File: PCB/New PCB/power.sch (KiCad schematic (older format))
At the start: 3 parts

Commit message: Updating Schematic for New PCB
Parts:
- added SW1: SWITCH_INV, ~, symbol SWITCH_INV
- gave numbers to parts that had none: 3
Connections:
- net labels added: DIO10, DIO8, DIO9
- wire segments 10 -> 14
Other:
- moved on the sheet: P1
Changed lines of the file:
@@
-EESchema Schematic File Version 2  date 5/26/2013 8:12:24 PM
+EESchema Schematic File Version 2  date 5/27/2013 10:54:42 AM
 LIBS:power
 LIBS:device
@@
 LIBS:MyLib
 LIBS:Test-cache
-EELAYER 25  0
+EELAYER 27 0
 EELAYER END
-$Descr A4 11700 8267
+$Descr A4 11693 8268
 encoding utf-8
 Sheet 2 3
@@
 $EndDescr
 $Comp
-L CONN_2 P?
+L CONN_2 P1
 U 1 1 51A2B2CF
-P 1150 1600
-F 0 "P?" V 1100 1600 40  0000 C CNN
-F 1 "BATT_CONN" V 1200 1600 40  0000 C CNN
-	1    1150 1600
+P 1950 1800
+F 0 "P1" V 1900 1800 40  0000 C CNN
+F 1 "BATT_CONN" V 2000 1800 40  0000 C CNN
+F 2 "" H 1950 1800 60  0001 C CNN
+F 3 "" H 1950 1800 60  0001 C CNN
+	1    1950 1800
 	-1   0    0    1
 $EndComp
 $Comp
-L VCC #PWR?
+L VCC #PWR06
 U 1 1 51A2B2CE
 P 4800 1350
-F 0 "#PWR?" H 4800 1450 30  0001 C CNN
+F 0 "#PWR06" H 4800 1450 30  0001 C CNN
 F 1 "VCC" H 4800 1450 30  0000 C CNN
+F 2 "" H 4800 1350 60  0001 C CNN
+F 3 "" H 4800 1350 60  0001 C CNN
 	1    4800 1350
 	1    0    0    -1
 $EndComp
 $Comp
-L GND #PWR?
+L GND #PWR07
 U 1 1 51A2B2CD
 P 4100 2350
-F 0 "#PWR?" H 4100 2350 30  0001 C CNN
+F 0 "#PWR07" H 4100 2350 30  0001 C CNN
 F 1 "GND" H 4100 2280 30  0001 C CNN
+F 2 "" H 4100 2350 60  0001 C CNN
+F 3 "" H 4100 2350 60  0001 C CNN
 	1    4100 2350
 	1    0    0    -1
 $EndComp
 $Comp
-L C C?
+L C C1
 U 1 1 51A2B2CC
 P 4650 1850
-F 0 "C?" H 4650 1950 40  0000 L CNN
+F 0 "C1" H 4650 1950 40  0000 L CNN
 F 1 "C" H 4656 1765 40  0000 L CNN
 F 2 "~" H 4688 1700 30  0000 C CNN
@@
 $EndComp
 $Comp
-L REG1117 IC?
+L REG1117 3.3V1
 U 1 1 51A2B2CB
 P 4100 1650
-F 0 "IC?" H 4000 1900 60  0000 C CNN
+F 0 "3.3V1" H 4000 1900 60  0000 C CNN
 F 1 "REG1117" H 4150 1750 60  0000 C CNN
+F 2 "" H 4100 1650 60  0001 C CNN
+F 3 "" H 4100 1650 60  0001 C CNN
 	1    4100 1650
 	1    0    0    -1
@@
 	3850 1650 3650 1650
 Wire Wire Line
-	1600 1700 1600 2100
+	2400 1900 2400 2300
 Connection ~ 4100 2150
 Wire Wire Line
-	1600 1500 1500 1500
+	2400 1700 2300 1700
 Wire Wire Line
-	1500 1700 1600 1700
+	2300 1900 2400 1900
+$Comp
+L SWITCH_INV SW1
+U 1 1 51A3B93F
+P 2900 1700
+F 0 "SW1" H 2700 1850 50  0000 C CNN
+F 1 "SWITCH_INV" H 2750 1550 50  0000 C CNN
+F 2 "~" H 2900 1700 60  0000 C CNN
+F 3 "~" H 2900 1700 60  0000 C CNN
+	1    2900 1700
+	1    0    0    -1
+$EndComp
+Wire Wire Line
+	2400 2300 4100 2300
+Connection ~ 4100 2300
+Wire Wire Line
+	3400 1800 3400 2300
+Connection ~ 3400 2300
+Wire Wire Line
+	3400 1600 3650 1600
+Wire Wire Line
+	3650 1600 3650 1650
+Text HLabel 6900 3050 0    60   UnSpc ~ 0
+DIO8
+Text HLabel 6900 3150 0    60   UnSpc ~ 0
+DIO9
+Text HLabel 6900 3250 0    60   UnSpc ~ 0
+DIO10
 $EndSCHEMATC

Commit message: updated schematic
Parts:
- removed 3.3V1: REG1117, symbol REG1117
- removed C1: C, ~, symbol C
- removed SW1: SWITCH_INV, ~, symbol SWITCH_INV
- added C? (x2): 10uF, symbol CP1
- added C? (x11): 0.1uF, symbol C
- added C? (x2): 47uF, symbol C
- added C?: 10uF, symbol C
- added D?: LED, symbol LED
- added IC2?: REG1117, ~, symbol REG1117
- added R?: 320, symbol R
- added R?: 10, symbol R
- added SW?: SPST, symbol SPST
- added U? (x2): V78W-500, symbol V78W-500
- added U?: REC5-4805SRWZ/H4/A, symbol REC5-4805SRWZ/H4/A
- added U?: DSPIC33EP512MC806, ~, symbol DSPIC33EP512MC806
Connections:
- net labels added: +5V, Mag1_V, Mag2_V, Motor_Power, VSS
- wire segments 14 -> 37
- no-connect marks 0 -> 2
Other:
- note added: "24V DC DC converters for Magnets"
- note added: "3.3V Linear Regulator"
- note added: "45V-52V Input"
- note added: "5V DC-DC Isolation Converter, 1A max"
- moved on the sheet: P1

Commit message: more updates
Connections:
- net labels added: MotorPower
- net labels removed: DIO10, DIO8, DIO9, Motor_Power
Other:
- moved on the sheet: C?, R?, U?B

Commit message: updated schematic
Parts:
- removed C? (x4): 0.1uF, symbol C
- removed C? (x2): 47uF, symbol C
- removed U? (x2): V78W-500, symbol V78W-500
- removed U?: REC5-4805SRWZ/H4/A, symbol REC5-4805SRWZ/H4/A
- added C1, C2: 200uF, symbol C
- added C10, C7, C8, C9: 0.1uF, symbol C
- added C11, C12: 500uF, symbol C
- added C3, C6: C, symbol C
- added D6, D7: DIODESCH, symbol DIODESCH
- added L1, L2: INDUCTOR, symbol INDUCTOR
- added R20, R21, R22, R23, R3, R4: R, symbol R
- added U2, U3: 1074HV, symbol 1074HV
- gave numbers to parts that had none: 16
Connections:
- net labels added: +24V, +48V
- net labels removed: Mag1_V, Mag2_V, MotorPower, VSS
- wire segments 37 -> 42
- no-connect marks 2 -> 0
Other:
- note added: "24V DC DC buck converter"
- note added: "5V DC DC buck converter"
- note added: "Could use the fixed 5V Version (LT1076-5)"
- note added: "RIPPLE CURRENT RATING ≥ IOUT/2"
- note added: "dsPIC power pins"
- note removed: "24V DC DC converters for Magnets"
- note removed: "5V DC-DC Isolation Converter, 1A max"
- moved on the sheet: C13, C14, C34, C35, D8, IC21, P1, R24, SW1

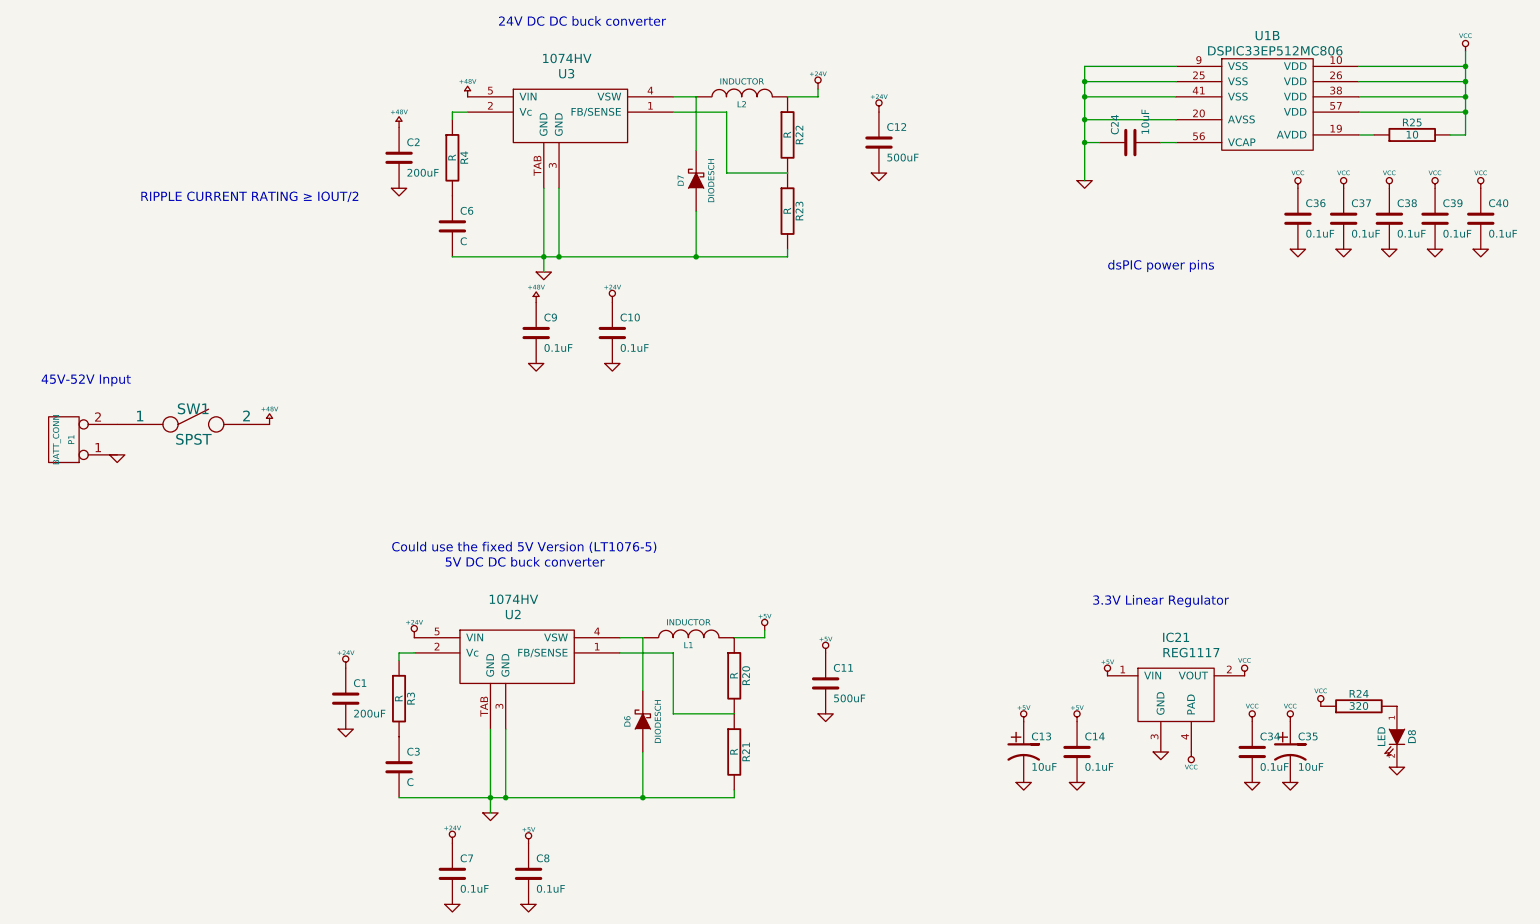
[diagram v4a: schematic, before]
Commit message: added notes to schematic
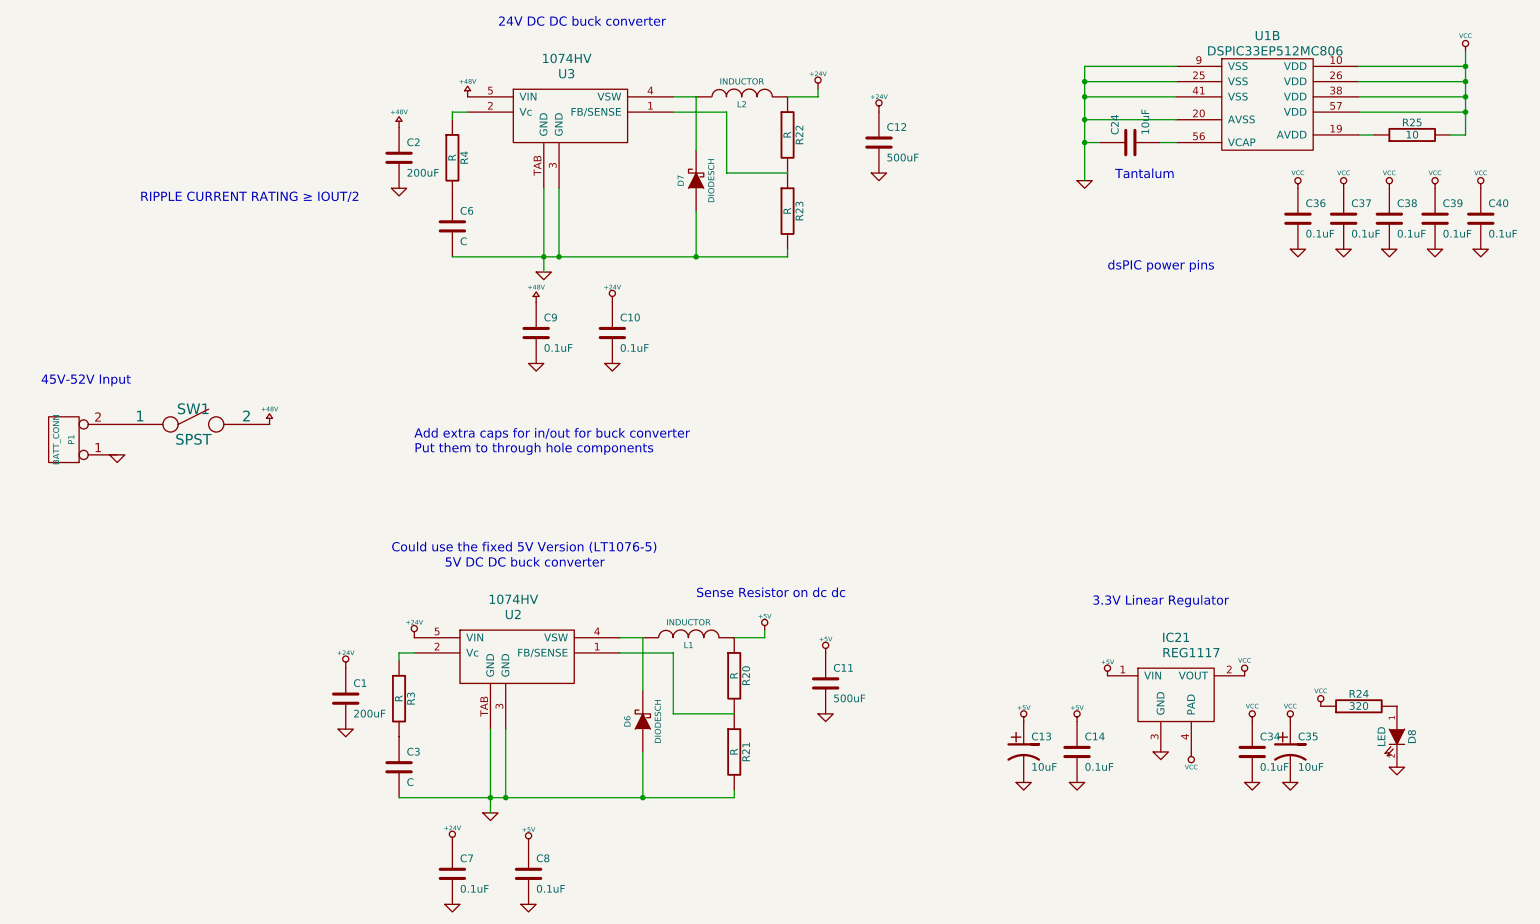
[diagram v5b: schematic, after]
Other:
- note added: "Add extra caps for in/out for buck converter\nPut them to through hole components"
- note added: "Sense Resistor on dc dc"
- note added: "Tantalum"
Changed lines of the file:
@@
-EESchema Schematic File Version 2
+EESchema Schematic File Version 2  date 6/2/2013 3:28:30 PM
 LIBS:power
 LIBS:device
@@
 Text Notes 3250 4150 0    60   ~ 0
 Could use the fixed 5V Version (LT1076-5)
+Text Notes 8000 1700 0    60   ~ 0
+Tantalum
+Text Notes 3400 3500 0    60   ~ 0
+Add extra caps for in/out for buck converter\nPut them to through hole components
+Text Notes 5250 4450 0    60   ~ 0
+Sense Resistor on dc dc
 $EndSCHEMATC

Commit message: updated schematic and netlist, added flyback diodes
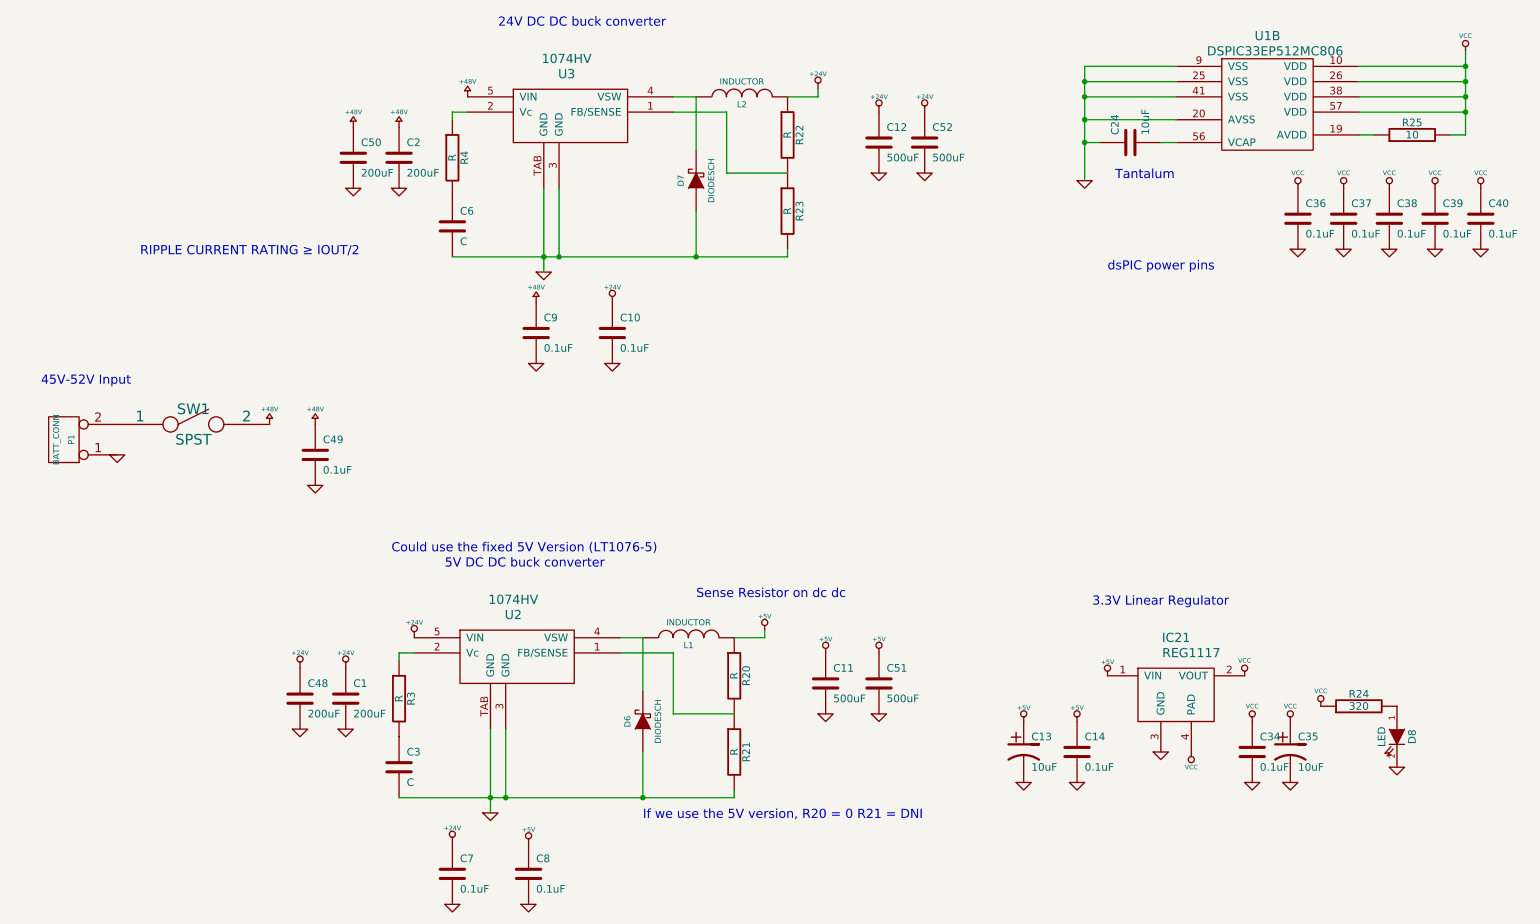
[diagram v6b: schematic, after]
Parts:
- added C48, C50: 200uF, symbol C
- added C49: 0.1uF, symbol C
- added C51, C52: 500uF, symbol C
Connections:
- net +24V: now also C48.1, C52.1
- net +48V: now also C49.1, C50.1
- net +5V: now also C51.1
- net GND: now also C48.2, C49.2, C50.2, C51.2, C52.2
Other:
- note added: "If we use the 5V version, R20 = 0 R21 = DNI"
- note removed: "Add extra caps for in/out for buck converter\nPut them to through hole components"

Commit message: order has been placed and confirmed, receipt in project folder
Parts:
- removed IC21: REG1117, ~, symbol REG1117
- added P20, P21, P22, P23, P24: CONN_1, symbol CONN_1
- added U6: TLV1117, ~, symbol TLV1117
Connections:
- net +24V: now also P21.1
- net +48V: now also P20.1
- net +5V: now also P22.1, U6.1 (VIN)
- net GND: now also P24.1, U6.3 (GND)
- net VCC: now also P23.1, U6.2 (VOUT), U6.4 (PAD)
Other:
- note added: "Test Points"
